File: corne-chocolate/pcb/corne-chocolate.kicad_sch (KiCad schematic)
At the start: 79 parts, among them J1 MJ-4PP-9, J2 Conn_01x04, P1 Conn_01x01, P2 Conn_01x01, SW10 SW_PUSH, SW11 SW_PUSH, SW12 SW_PUSH, SW14 SW_PUSH, SW15 SW_PUSH, SW16 SW_PUSH, SW17 SW_PUSH, SW18 SW_PUSH, SW19 SW_PUSH, SW2 SW_PUSH, SW20 SW_PUSH, SW21 SW_PUSH, SW3 SW_PUSH, SW4 SW_PUSH, SW5 SW_PUSH, SW6 SW_PUSH, SW8 SW_PUSH, SW9 SW_PUSH, U1 ProMicro

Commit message: starts component review
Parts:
- removed D10, D11, D12, D14, D15, D16, D17, D18, D19, D2, D20, D21, D3, D4, D5, D6, D8, D9: D, kbd:D3_SMD, symbol Device:D
- added D10, D11, D12, D14, D15, D16, D17, D18, D19, D2, D20, D21, D3, D4, D5, D6, D8, D9: 1N4148W, kbd:D_SOD-123, symbol Diode:1N4148W
- SW14: footprint (none) -> kbd:ChocV1_V2_Hotswap; supplier (none) -> Digikey
- U1: footprint (none) -> kbd:ProMicro_v2_1side; supplier (none) -> Digikey; supplier pn (none) -> 1568-DEV-15795-ND
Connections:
- net row0: now also D2.1 (K), D3.1 (K), D4.1 (K), D5.1 (K), D6.1 (K)
- net row1: now also D10.1 (K), D11.1 (K), D12.1 (K), D8.1 (K), D9.1 (K)
- net row2: now also D14.1 (K), D15.1 (K), D16.1 (K), D17.1 (K), D18.1 (K)
- net row3: now also D19.1 (K), D20.1 (K), D21.1 (K)
- net at SW2.2: now also D2.2 (A)
- net at SW3.2: now also D3.2 (A)
- net at SW4.2: now also D4.2 (A)
- net at SW5.2: now also D5.2 (A)
- net at SW6.2: now also D6.2 (A)
- net at SW8.2: now also D8.2 (A)
- net at SW9.2: now also D9.2 (A)
- net at SW10.2: now also D10.2 (A)
- net at SW11.2: now also D11.2 (A)
- net at SW12.2: now also D12.2 (A)
- net at SW14.2: now also D14.2 (A)
- net at SW15.2: now also D15.2 (A)
- net at SW16.2: now also D16.2 (A)
- net at SW17.2: now also D17.2 (A)
- net at SW18.2: now also D18.2 (A)
- net at SW20.2: now also D20.2 (A)
- net at SW21.2: now also D21.2 (A)
- net at SW19.2: now also D19.2 (A)

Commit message: footprint verified, list of components with their vendors sites
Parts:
- D10, D11, D12, D14, D15, D16, D17, D18, D19, D2, D20, D21, D3, D4, D5, D6, D8, D9: fp check (none) -> Y; vendor site (none) -> https://www.digikey.com/en/products/detail/diodes-incorpora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
- J1: fp check (none) -> ?; supplier (none) -> Digikey; supplier pn (none) -> SJ2-3574A-SMT-TR; vendor site (none) -> https://www.digikey.com/en/products/detail/cui-devices/SJ2-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
- J2: fp check (none) -> Y; supplier pn (none) -> -; vendor site (none) -> https://www.amazon.com/-/es/pantalla-pulgadas-SSD1306-contr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
- L10, L11, L12, L14, L15, L16, L17, L18, L19, L2, L20, L21, L22, L23, L24, L25, L26, L27, L3, L4, L5, L6, L8, L9: fp check (none) -> ?; supplier (none) -> Digikey; supplier pn (none) -> 1528-1710-ND; vendor site (none) -> https://www.digikey.com/en/products/detail/adafruit-industr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
- RSW1: fp check (none) -> Y; supplier (none) -> Digikey; supplier pn (none) -> PTS636 SM43 SMTR LFS; vendor site (none) -> https://www.digikey.com/en/products/detail/c-k/PTS636-SM43-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
- SW10, SW11, SW12, SW15, SW16, SW17, SW18, SW19, SW2, SW20, SW21, SW3, SW4, SW5, SW6, SW8, SW9: fp check (none) -> Y; vendor site (none) -> https://www.digikey.com/en/products/detail/adafruit-industr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
- SW14: fp check (none) -> Y; supplier pn (none) -> 1528-5118-ND; vendor site (none) -> https://www.digikey.com/en/products/detail/adafruit-industr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
- U1: fp check (none) -> Y

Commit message: updates part list
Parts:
- D10, D11, D12, D14, D15, D16, D17, D18, D19, D2, D20, D21, D3, D4, D5, D6, D8, D9: item qty (none) -> 100; supplier Digikey -> Amazon; supplier pn 1N4148W-FDICT-ND -> B09DR5KFXM; vendor site https://www.digikey.com/en/products/detail/diodes-incorpora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 -> https://www.amazon.com/Adafruit-Industries-1N4148-SOD-123-D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
- J1: item qty (none) -> 10; supplier Digikey -> Amazon; supplier pn SJ2-3574A-SMT-TR -> B07KY7CJCJ; vendor site https://www.digikey.com/en/products/detail/cui-devices/SJ2-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 -> https://www.amazon.com/uxcell-Audio-Connector-Mount-Socket/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
- J2: item qty (none) -> 10; supplier (none) -> Amazon; supplier pn - -> B0925V1DZK
- L10, L11, L12, L14, L15, L16, L17, L18, L19, L2, L20, L21, L22, L23, L24, L25, L26, L27, L3, L4, L5, L6, L8, L9: item qty (none) -> 6; supplier Digikey -> Amazon; supplier pn 1528-1710-ND -> ‎B0B7H7NXMB; vendor site https://www.digikey.com/en/products/detail/adafruit-industr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 -> https://www.amazon.com/AITRIP-SSD1306-Character-Compatible-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
- RSW1: item qty (none) -> 50; supplier Digikey -> Amazon; supplier pn PTS636 SM43 SMTR LFS -> B07H9ZSZD4; vendor site https://www.digikey.com/en/products/detail/c-k/PTS636-SM43-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 -> https://www.amazon.com/-/es/uxcell-0-118x0-236x0-197-Peque%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
- SW10, SW11, SW12, SW14, SW15, SW16, SW17, SW18, SW19, SW2, SW20, SW21, SW3, SW4, SW5, SW6, SW8, SW9: item qty (none) -> 100; supplier Digikey -> Amazon; supplier pn 1528-5118-ND -> B0CPVJLMDJ; vendor site https://www.digikey.com/en/products/detail/adafruit-industr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 -> https://www.amazon.com/100Pieces-Chocolate-Switches-Accesso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

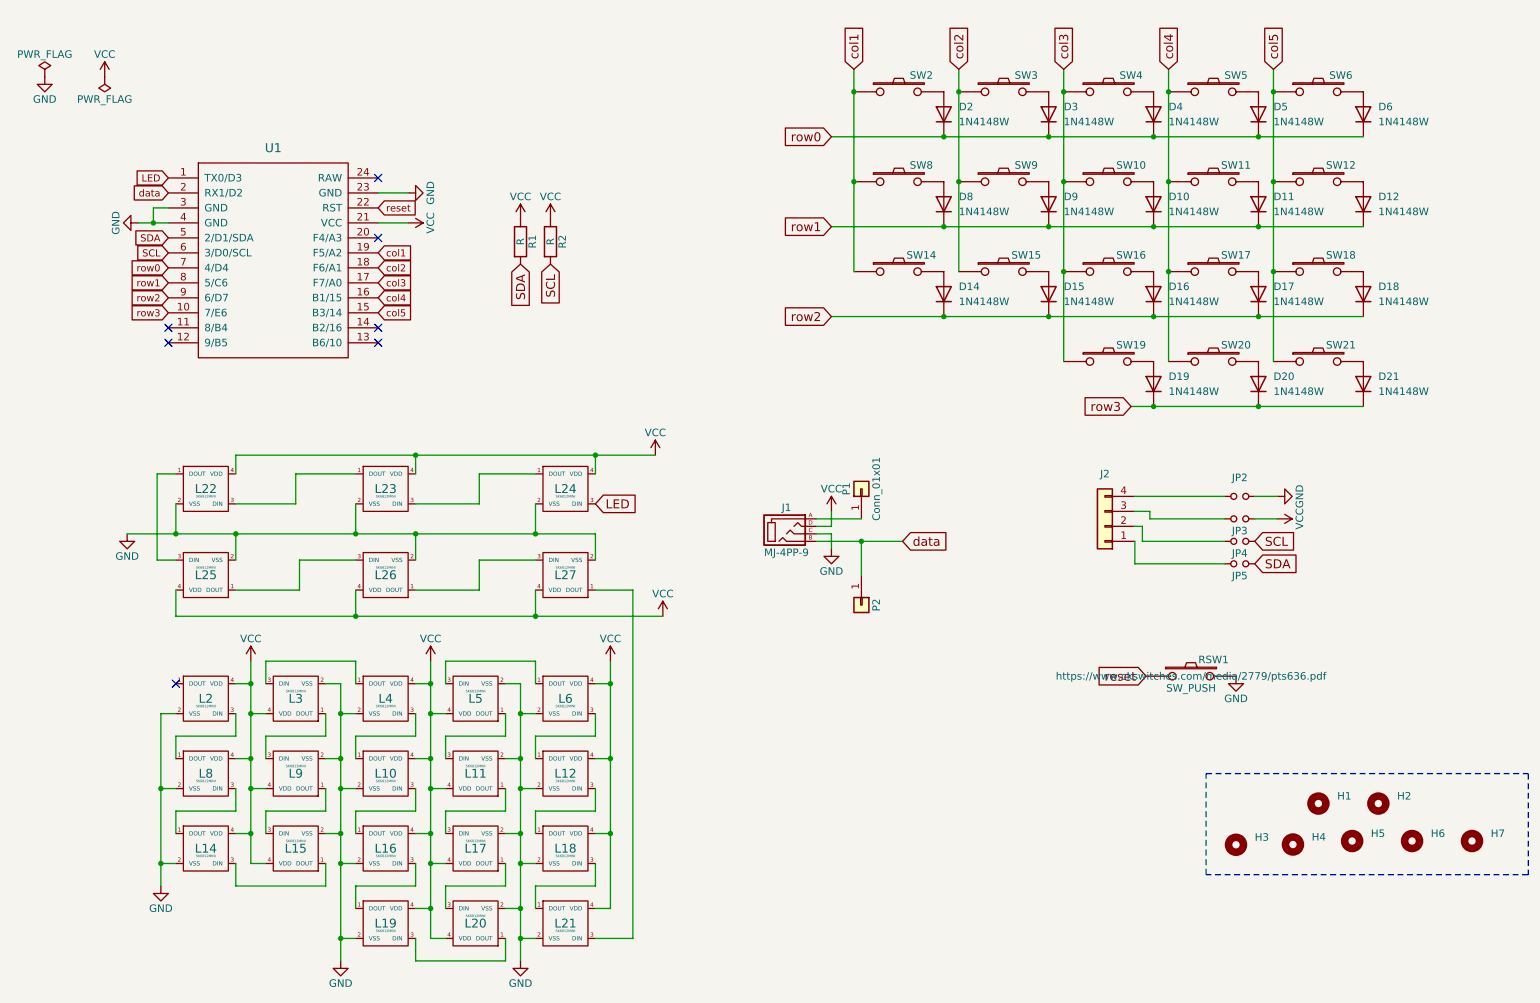
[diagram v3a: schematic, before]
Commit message: switch to nrf52840 micro. All items from amazon
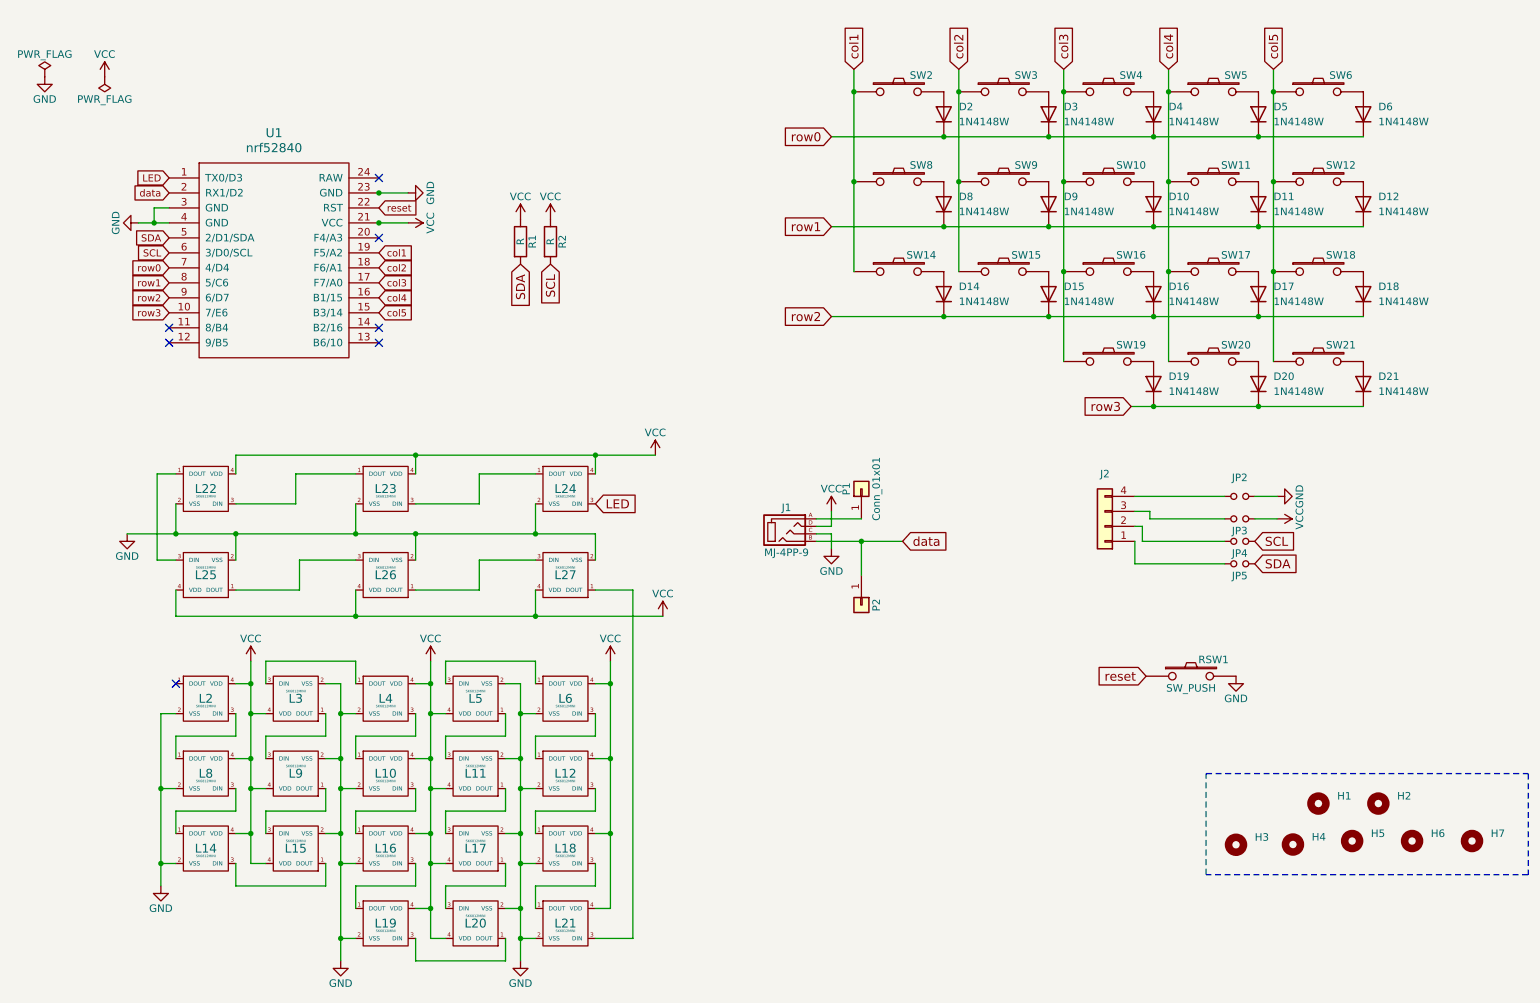
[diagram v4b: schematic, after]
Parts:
- removed U1: ProMicro, kbd:ProMicro_v2_1side, symbol kbd:ProMicro
- added U1: nrf52840, kbd:nrf52840, symbol kbd:nrf52840
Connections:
- net GND: now also U1.23 (GND), U1.3 (GND), U1.4 (GND)
- net LED: now also U1.1 (TX0/D3)
- net SCL: now also U1.6 (3/D0/SCL)
- net SDA: now also U1.5 (2/D1/SDA)
- net VCC: now also U1.21 (VCC)
- net col1: now also U1.19 (F5/A2)
- net col2: now also U1.18 (F6/A1)
- net col3: now also U1.17 (F7/A0)
- net col4: now also U1.16 (B1/15)
- net col5: now also U1.15 (B3/14)
- net data: now also U1.2 (RX1/D2)
- net reset: now also U1.22 (RST)
- net row0: now also U1.7 (4/D4)
- net row1: now also U1.8 (5/C6)
- net row2: now also U1.9 (6/D7)
- net row3: now also U1.10 (7/E6)

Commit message: adds right keyboard
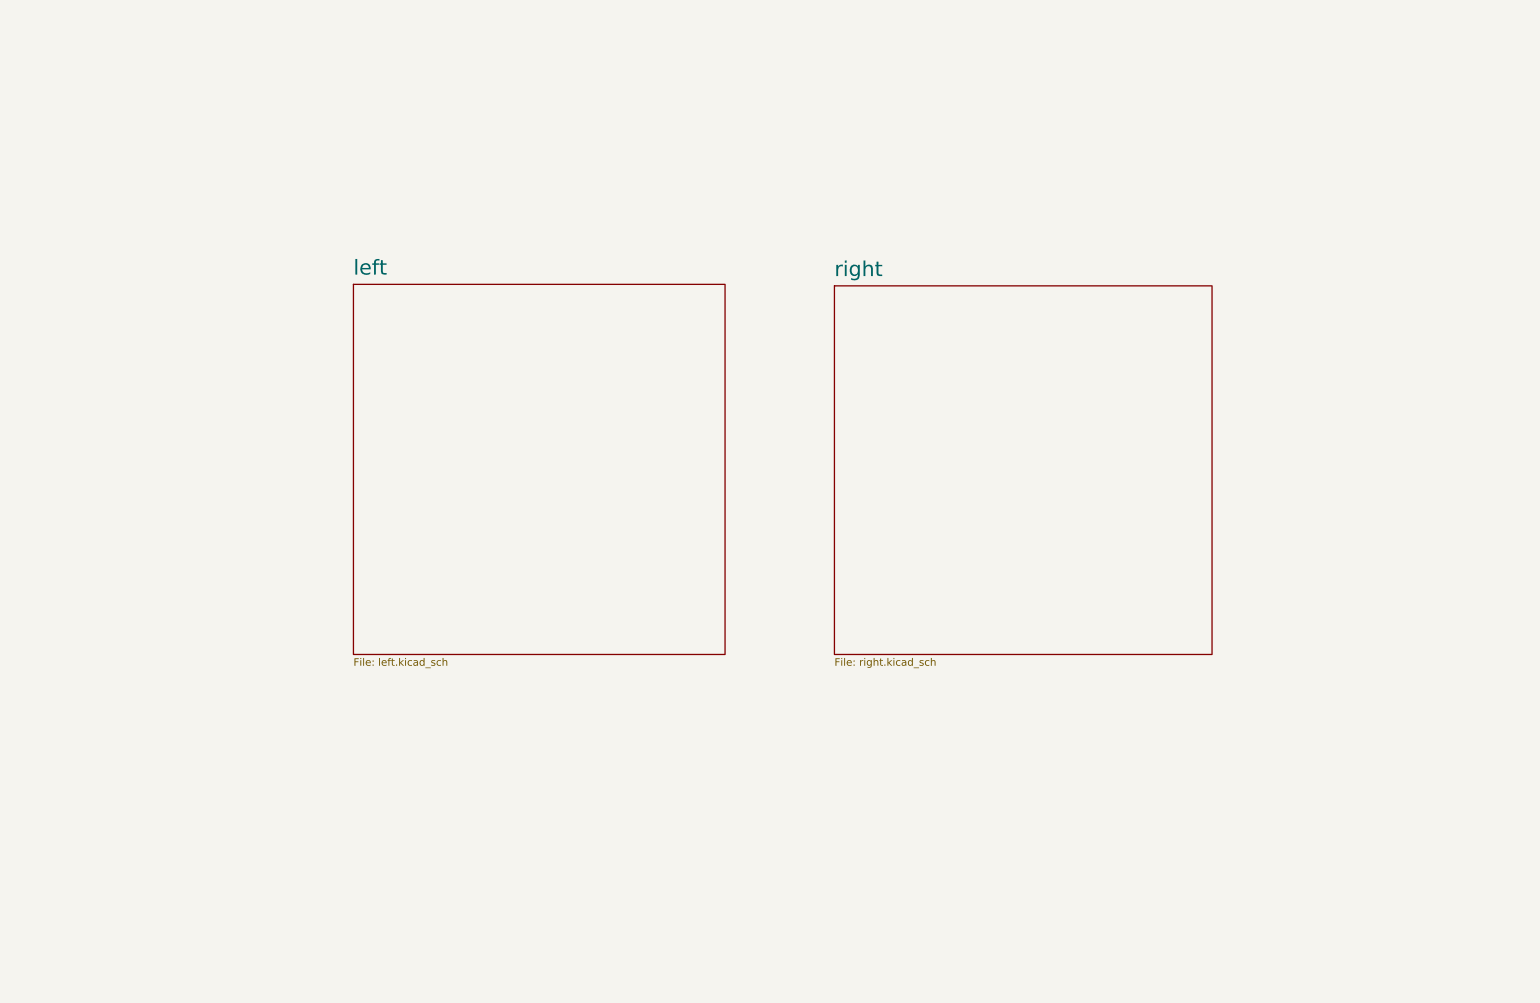
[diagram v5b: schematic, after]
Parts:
- removed D10, D11, D12, D14, D15, D16, D17, D18, D19, D2, D20, D21, D3, D4, D5, D6, D8, D9: 1N4148W, kbd:D_SOD-123, symbol Diode:1N4148W
- removed H1, H2: MountingHole, MountingHole:MountingHole_2.2mm_M2_ISO14580, symbol Mechanical:MountingHole
- removed H3, H4, H5, H6, H7: MountingHole, MountingHole:MountingHole_4.3mm_M4_ISO14580, symbol Mechanical:MountingHole
- removed J1: MJ-4PP-9, kbd:MJ-4PP-9_1side, symbol kbd:MJ-4PP-9
- removed J2: Conn_01x04, kbd:OLED_1side, symbol Connector_Generic:Conn_01x04
- removed JP2, JP3, JP4, JP5: Device:Jumper_NO_Small, kbd:Jumper, symbol kbd:Jumper_NO_Small-Device
- removed L10, L11, L12, L14, L15, L16, L17, L18, L19, L2, L20, L21, L3, L4, L5, L6, L8, L9: SK6812MINI, kbd:YS-SK6812MINI-E, symbol kbd:SK6812MINI
- removed L22, L23, L24, L25, L26, L27: SK6812MINI, kbd:SK6812MINI_underglow_rev, symbol kbd:SK6812MINI
- removed P1, P2: Conn_01x01, kbd:1pin_conn, symbol Connector_Generic:Conn_01x01
- removed R1, R2: R, kbd:R, symbol Device:R
- removed RSW1: SW_PUSH, kbd:ResetSW_1side, symbol kbd:SW_PUSH
- removed SW10, SW11, SW12, SW14, SW15, SW16, SW17, SW18, SW19, SW2, SW20, SW3, SW4, SW5, SW6, SW8, SW9: SW_PUSH, kbd:ChocV1_V2_Hotswap, symbol kbd:SW_PUSH
- removed SW21: SW_PUSH, kbd:ChocV1_V2_Hotswap_1.5u, symbol kbd:SW_PUSH
- removed U1: nrf52840, kbd:nrf52840, symbol kbd:nrf52840
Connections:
- no-connect marks 7 -> 0
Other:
- added sheet left (left.kicad_sch)
- added sheet right (right.kicad_sch)
- company: foostan -> (none)
